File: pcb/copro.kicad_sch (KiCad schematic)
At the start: 6 parts, among them U10 74HC245, U2 ATmega1284-P, U6 74HC245, U7 74HC04, U8 74HC02, U9 74HC245

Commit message: WIP schematic
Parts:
- renumbered U8 to U37, U2 to U38, U10 to U39, U9 to U40, U6 to U41, U7 to U9
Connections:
- net VCC renamed +5V

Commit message: WIP PCB
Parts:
- renumbered U37 to U?, U41 to U?, U38 to U?, U39 to U?, U40 to U?, U9 to U?

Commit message: wip schematic
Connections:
- net +5V: now also U?.1 (A->B), U?.1 (A->B)
- net GND: no longer U?.1 (A->B), U?.1 (A->B)
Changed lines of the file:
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@@
-	(wire
-		(pts
-			(xy 107.95 93.98) (xy 107.95 97.79)
-		)
-		(stroke
-			(width 0)
-			(type default)
-		)
-	)
 	(wire
 		(pts
@@
 		(pts
 			(xy 50.8 154.94) (xy 53.34 154.94)
-		)
-		(stroke
-			(width 0)
-			(type default)
-		)
-	)
-	(wire
-		(pts
-			(xy 69.85 58.42) (xy 69.85 54.61)
 		)
 		(stroke
@@
 	)
 	(symbol
-		(lib_id "power:GND")
-		(at 107.95 97.79 0)
-		(unit 1)
-		(exclude_from_sim no)
-		(in_bom yes)
-		(on_board yes)
-		(dnp no)
-		(property "Reference" "#PWR?"
-			(at 107.95 104.14 0)
-			(effects
-				(font
-					(size 1.27 1.27)
-				)
-				(hide yes)
-			)
-		)
-		(property "Value" "GND"
-			(at 107.95 101.6 0)
-			(effects
-				(font
-					(size 1.27 1.27)
-				)
-			)
-		)
-		(property "Footprint" ""
-			(at 107.95 97.79 0)
-			(effects
-				(font
-					(size 1.27 1.27)
-				)
-				(hide yes)
-			)
-		)
-		(property "Datasheet" ""
-			(at 107.95 97.79 0)
-			(effects
-				(font
-					(size 1.27 1.27)
-				)
-				(hide yes)
-			)
-		)
-		(property "Description" "Power symbol creates a global label with name \"GND\" , ground"
-			(at 107.95 97.79 0)
-			(effects
-				(font
-					(size 1.27 1.27)
-				)
-				(hide yes)
-			)
-		)
-		(pin "1"
-		)
-		(instances
-			(project "fnx51"
-				(path "/e63e39d7-6ac0-4ffd-8aa3-1841a4541b55/90e1f016-3c60-4383-aa8d-def9977ac47b/81e744bc-21ac-4a4e-ae92-db4ae42ab216"
-					(reference "#PWR?")
-					(unit 1)
-				)
-			)
-		)
-	)
-	(symbol
 		(lib_id "MCU_Microchip_ATmega:ATmega1284-P")
 		(at 50.8 207.01 0)
@@
 	)
 	(symbol
-		(lib_id "power:GND")
-		(at 69.85 58.42 0)
+		(lib_id "power:+5V")
+		(at 107.95 93.98 0)
 		(unit 1)
 		(exclude_from_sim no)
@@
 		(on_board yes)
 		(dnp no)
-		(property "Reference" "#PWR?"
-			(at 69.85 64.77 0)
-			(effects
-				(font
-					(size 1.27 1.27)
-				)
-				(hide yes)
-			)
-		)
-		(property "Value" "GND"
-			(at 69.85 62.23 0)
+		(property "Reference" "#PWR04"
+			(at 107.95 97.79 0)
+			(effects
+				(font
+					(size 1.27 1.27)
+				)
+				(hide yes)
+			)
+		)
+		(property "Value" "+5V"
+			(at 104.14 92.71 0)
 			(effects
 				(font
@@
 		)
 		(property "Footprint" ""
-			(at 69.85 58.42 0)
+			(at 107.95 93.98 0)
 			(effects
 				(font
@@
 		)
 		(property "Datasheet" ""
-			(at 69.85 58.42 0)
-			(effects
-				(font
-					(size 1.27 1.27)
-				)
-				(hide yes)
-			)
-		)
-		(property "Description" "Power symbol creates a global label with name \"GND\" , ground"
-			(at 69.85 58.42 0)
+			(at 107.95 93.98 0)
+			(effects
+				(font
+					(size 1.27 1.27)
+				)
+				(hide yes)
+			)
+		)
+		(property "Description" "Power symbol creates a global label with name \"+5V\""
+			(at 107.95 93.98 0)
 			(effects
 				(font
@@
 			(project "fnx51"
 				(path "/e63e39d7-6ac0-4ffd-8aa3-1841a4541b55/90e1f016-3c60-4383-aa8d-def9977ac47b/81e744bc-21ac-4a4e-ae92-db4ae42ab216"
-					(reference "#PWR?")
+					(reference "#PWR04")
 					(unit 1)
 				)
@@
 				)
 			)
+		)
+	)
+	(symbol
+		(lib_id "power:+5V")
+		(at 69.85 54.61 0)
+		(unit 1)
+		(exclude_from_sim no)
+		(in_bom yes)
+		(on_board yes)
+		(dnp no)
+		(property "Reference" "#PWR03"
+			(at 69.85 58.42 0)
+			(effects
+				(font
+					(size 1.27 1.27)
+				)
+				(hide yes)
+			)
+		)
+		(property "Value" "+5V"
+			(at 66.04 53.34 0)
+			(effects
+				(font
+					(size 1.27 1.27)
+				)
+			)
+		)
+		(property "Footprint" ""
+			(at 69.85 54.61 0)
+			(effects
+				(font
+					(size 1.27 1.27)
+				)
+				(hide yes)
+			)
+		)
+		(property "Datasheet" ""
+			(at 69.85 54.61 0)
+			(effects
+				(font
+					(size 1.27 1.27)
+				)
+				(hide yes)
+			)
+		)
+		(property "Description" "Power symbol creates a global label with name \"+5V\""
+			(at 69.85 54.61 0)
+			(effects
+				(font
+					(size 1.27 1.27)
+				)
+				(hide yes)
+			)
+		)
+		(pin "1"
+		)
+		(instances
+			(project "fnx51"
+				(path "/e63e39d7-6ac0-4ffd-8aa3-1841a4541b55/90e1f016-3c60-4383-aa8d-def9977ac47b/81e744bc-21ac-4a4e-ae92-db4ae42ab216"
+					(reference "#PWR03")
+					(unit 1)
+				)
+			)

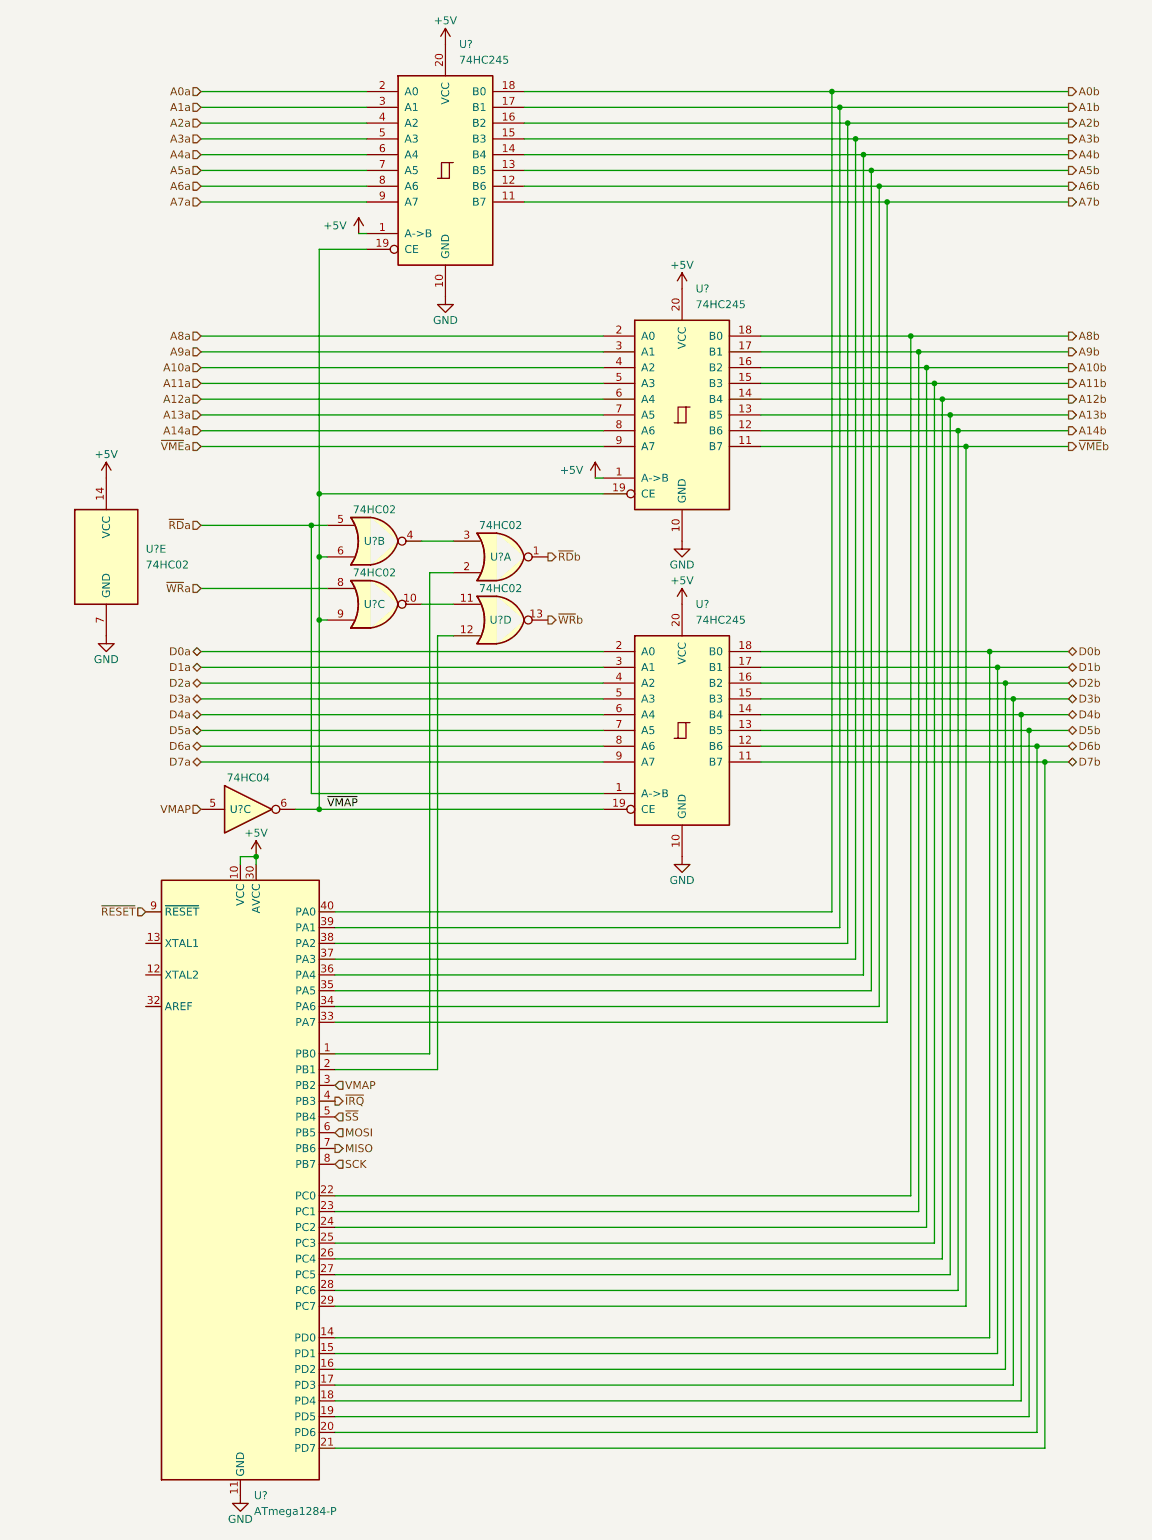
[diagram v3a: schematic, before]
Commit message: PCB: add reset circuit, xtal
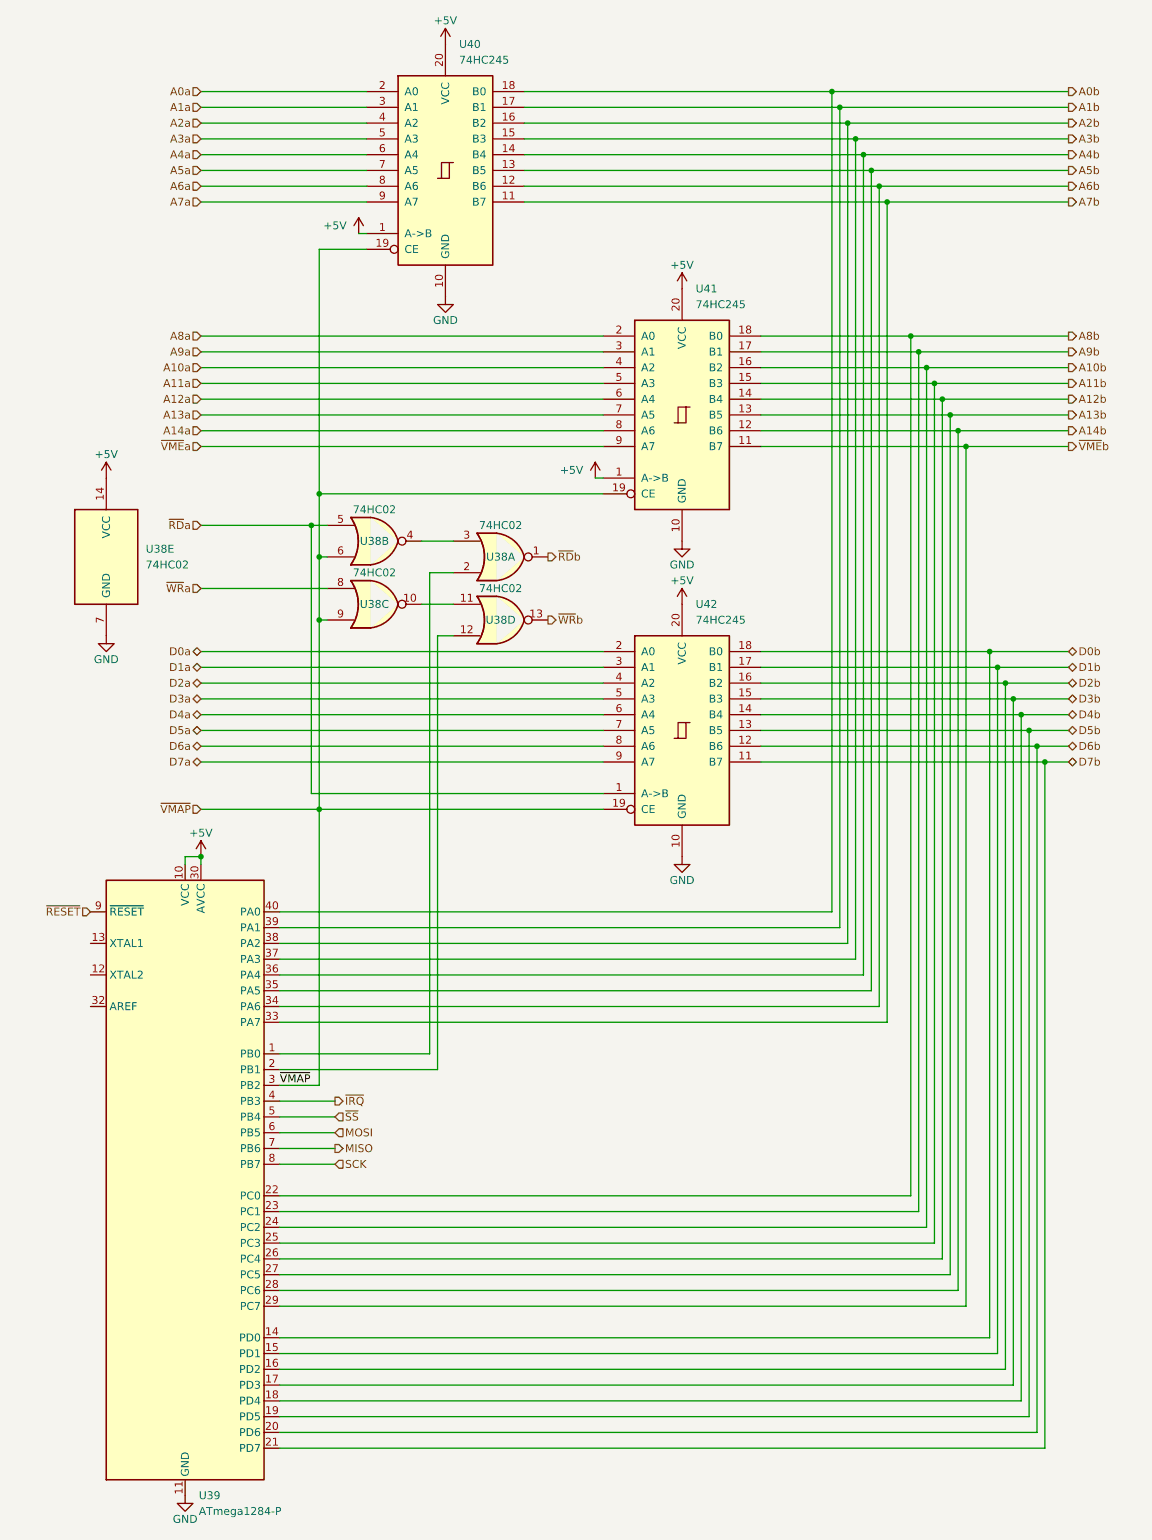
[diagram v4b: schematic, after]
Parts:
- removed U?: 74HC04, symbol 74xx:74HC04
- gave numbers to parts that had none: 5
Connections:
- net VMAP is gone; now on net ~{VMAP}: U39.3 (PB2)
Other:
- moved on the sheet: U39

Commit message: WIP schematic
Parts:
- renumbered U38 to U39, U39 to U40, U40 to U41, U41 to U42, U42 to U43
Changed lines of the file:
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@@
 		(on_board yes)
 		(dnp no)
-		(property "Reference" "U38"
+		(property "Reference" "U39"
 			(at 72.39 104.14 0)
 			(effects
@@
 			(project ""
 				(path "/e63e39d7-6ac0-4ffd-8aa3-1841a4541b55/90e1f016-3c60-4383-aa8d-def9977ac47b/81e744bc-21ac-4a4e-ae92-db4ae42ab216"
-					(reference "U38")
+					(reference "U39")
 					(unit 2)
 				)
@@
 		(on_board yes)
 		(dnp no)
-		(property "Reference" "U38"
+		(property "Reference" "U39"
 			(at 92.71 116.84 0)
 			(effects
@@
 			(project ""
 				(path "/e63e39d7-6ac0-4ffd-8aa3-1841a4541b55/90e1f016-3c60-4383-aa8d-def9977ac47b/81e744bc-21ac-4a4e-ae92-db4ae42ab216"
-					(reference "U38")
+					(reference "U39")
 					(unit 4)
 				)
@@
 		(on_board yes)
 		(dnp no)
-		(property "Reference" "#PWR0132"
+		(property "Reference" "#PWR0147"
 			(at 121.92 161.29 0)
 			(effects
@@
 			(project ""
 				(path "/e63e39d7-6ac0-4ffd-8aa3-1841a4541b55/90e1f016-3c60-4383-aa8d-def9977ac47b/81e744bc-21ac-4a4e-ae92-db4ae42ab216"
-					(reference "#PWR0132")
+					(reference "#PWR0147")
 					(unit 1)
 				)
@@
 		(on_board yes)
 		(dnp no)
-		(property "Reference" "#PWR0127"
+		(property "Reference" "#PWR0142"
 			(at 83.82 71.12 0)
 			(effects
@@
 			(project "fnx51"
 				(path "/e63e39d7-6ac0-4ffd-8aa3-1841a4541b55/90e1f016-3c60-4383-aa8d-def9977ac47b/81e744bc-21ac-4a4e-ae92-db4ae42ab216"
-					(reference "#PWR0127")
+					(reference "#PWR0142")
 					(unit 1)
 				)
@@
 		(on_board yes)
 		(dnp no)
-		(property "Reference" "U38"
+		(property "Reference" "U39"
 			(at 72.39 114.3 0)
 			(effects
@@
 			(project ""
 				(path "/e63e39d7-6ac0-4ffd-8aa3-1841a4541b55/90e1f016-3c60-4383-aa8d-def9977ac47b/81e744bc-21ac-4a4e-ae92-db4ae42ab216"
-					(reference "U38")
+					(reference "U39")
 					(unit 3)
 				)
@@
 		(on_board yes)
 		(dnp no)
-		(property "Reference" "#PWR0130"
+		(property "Reference" "#PWR0145"
 			(at 121.92 110.49 0)
 			(effects
@@
 			(project "fnx51"
 				(path "/e63e39d7-6ac0-4ffd-8aa3-1841a4541b55/90e1f016-3c60-4383-aa8d-def9977ac47b/81e744bc-21ac-4a4e-ae92-db4ae42ab216"
-					(reference "#PWR0130")
+					(reference "#PWR0145")
 					(unit 1)
 				)
@@
 		(dnp no)
 		(fields_autoplaced yes)
-		(property "Reference" "U42"
+		(property "Reference" "U43"
 			(at 124.1141 114.3 0)
 			(effects
@@
 			(project ""
 				(path "/e63e39d7-6ac0-4ffd-8aa3-1841a4541b55/90e1f016-3c60-4383-aa8d-def9977ac47b/81e744bc-21ac-4a4e-ae92-db4ae42ab216"
-					(reference "U42")
+					(reference "U43")
 					(unit 1)
 				)
@@
 		(dnp no)
 		(fields_autoplaced yes)
-		(property "Reference" "U39"
+		(property "Reference" "U40"
 			(at 44.1041 257.81 0)
 			(effects
@@
 			(project ""
 				(path "/e63e39d7-6ac0-4ffd-8aa3-1841a4541b55/90e1f016-3c60-4383-aa8d-def9977ac47b/81e744bc-21ac-4a4e-ae92-db4ae42ab216"
-					(reference "U39")
+					(reference "U40")
 					(unit 1)
 				)
@@
 		(on_board yes)
 		(dnp no)
-		(property "Reference" "#PWR0128"
+		(property "Reference" "#PWR0143"
 			(at 107.95 97.79 0)
 			(effects
@@
 			(project "fnx51"
 				(path "/e63e39d7-6ac0-4ffd-8aa3-1841a4541b55/90e1f016-3c60-4383-aa8d-def9977ac47b/81e744bc-21ac-4a4e-ae92-db4ae42ab216"
-					(reference "#PWR0128")
+					(reference "#PWR0143")
 					(unit 1)
 				)
@@
 		(on_board yes)
 		(dnp no)
-		(property "Reference" "#PWR0126"
+		(property "Reference" "#PWR0141"
 			(at 83.82 27.94 0)
 			(effects
@@
 			(project "fnx51"
 				(path "/e63e39d7-6ac0-4ffd-8aa3-1841a4541b55/90e1f016-3c60-4383-aa8d-def9977ac47b/81e744bc-21ac-4a4e-ae92-db4ae42ab216"
-					(reference "#PWR0126")
+					(reference "#PWR0141")
 					(unit 1)
 				)
@@
 		(on_board yes)
 		(dnp no)
-		(property "Reference" "U38"
+		(property "Reference" "U39"
 			(at 92.71 106.68 0)
 			(effects
@@
 			(project ""
 				(path "/e63e39d7-6ac0-4ffd-8aa3-1841a4541b55/90e1f016-3c60-4383-aa8d-def9977ac47b/81e744bc-21ac-4a4e-ae92-db4ae42ab216"
-					(reference "U38")
+					(reference "U39")
 					(unit 1)
 				)
@@
 		(on_board yes)
 		(dnp no)
-		(property "Reference" "#PWR0131"
+		(property "Reference" "#PWR0146"
 			(at 121.92 118.11 0)
 			(effects
@@
 			(project ""
 				(path "/e63e39d7-6ac0-4ffd-8aa3-1841a4541b55/90e1f016-3c60-4383-aa8d-def9977ac47b/81e744bc-21ac-4a4e-ae92-db4ae42ab216"
-					(reference "#PWR0131")
+					(reference "#PWR0146")
 					(unit 1)
 				)
@@
 		(dnp no)
 		(fields_autoplaced yes)
-		(property "Reference" "U40"
+		(property "Reference" "U41"
 			(at 86.0141 24.13 0)
 			(effects
@@
 			(project "fnx51"
 				(path "/e63e39d7-6ac0-4ffd-8aa3-1841a4541b55/90e1f016-3c60-4383-aa8d-def9977ac47b/81e744bc-21ac-4a4e-ae92-db4ae42ab216"
-					(reference "U40")
+					(reference "U41")
 					(unit 1)
 				)
@@
 		(dnp no)
 		(fields_autoplaced yes)
-		(property "Reference" "U38"
+		(property "Reference" "U39"
 			(at 35.56 105.4099 0)
 			(effects
@@
 			(project ""
 				(path "/e63e39d7-6ac0-4ffd-8aa3-1841a4541b55/90e1f016-3c60-4383-aa8d-def9977ac47b/81e744bc-21ac-4a4e-ae92-db4ae42ab216"
-					(reference "U38")
+					(reference "U39")
 					(unit 5)
 				)
@@
 		(on_board yes)
 		(dnp no)
-		(property "Reference" "#PWR0125"
+		(property "Reference" "#PWR0140"
 			(at 69.85 58.42 0)
 			(effects
@@
 			(project "fnx51"
 				(path "/e63e39d7-6ac0-4ffd-8aa3-1841a4541b55/90e1f016-3c60-4383-aa8d-def9977ac47b/81e744bc-21ac-4a4e-ae92-db4ae42ab216"
-					(reference "#PWR0125")
+					(reference "#PWR0140")
 					(unit 1)
 				)
@@
 		(on_board yes)
 		(dnp no)
-		(property "Reference" "#PWR0121"
+		(property "Reference" "#PWR0136"
 			(at 29.21 97.79 0)
 			(effects
@@
 			(project "fnx51"
 				(path "/e63e39d7-6ac0-4ffd-8aa3-1841a4541b55/90e1f016-3c60-4383-aa8d-def9977ac47b/81e744bc-21ac-4a4e-ae92-db4ae42ab216"
-					(reference "#PWR0121")
+					(reference "#PWR0136")
 					(unit 1)
 				)
@@
 		(dnp no)
 		(fields_autoplaced yes)
-		(property "Reference" "U41"
+		(property "Reference" "U42"
 			(at 124.1141 63.5 0)
 			(effects
@@
 			(project "fnx51"
 				(path "/e63e39d7-6ac0-4ffd-8aa3-1841a4541b55/90e1f016-3c60-4383-aa8d-def9977ac47b/81e744bc-21ac-4a4e-ae92-db4ae42ab216"
-					(reference "U41")
+					(reference "U42")
 					(unit 1)
 				)
@@
 		(on_board yes)
 		(dnp no)
-		(property "Reference" "#PWR0123"
+		(property "Reference" "#PWR0138"
 			(at 41.91 264.16 0)
 			(effects
@@
 			(project "fnx51"
 				(path "/e63e39d7-6ac0-4ffd-8aa3-1841a4541b55/90e1f016-3c60-4383-aa8d-def9977ac47b/81e744bc-21ac-4a4e-ae92-db4ae42ab216"
-					(reference "#PWR0123")
+					(reference "#PWR0138")
 					(unit 1)
 				)
@@
 		(on_board yes)
 		(dnp no)
-		(property "Reference" "#PWR0124"
+		(property "Reference" "#PWR0139"
 			(at 44.45 158.75 0)
 			(effects
@@
 			(project "fnx51"
 				(path "/e63e39d7-6ac0-4ffd-8aa3-1841a4541b55/90e1f016-3c60-4383-aa8d-def9977ac47b/81e744bc-21ac-4a4e-ae92-db4ae42ab216"
-					(reference "#PWR0124")
+					(reference "#PWR0139")
 					(unit 1)
 				)
@@
 		(on_board yes)
 		(dnp no)
-		(property "Reference" "#PWR0122"
+		(property "Reference" "#PWR0137"
 			(at 29.21 125.73 0)
 			(effects
@@
 			(project "fnx51"
 				(path "/e63e39d7-6ac0-4ffd-8aa3-1841a4541b55/90e1f016-3c60-4383-aa8d-def9977ac47b/81e744bc-21ac-4a4e-ae92-db4ae42ab216"
-					(reference "#PWR0122")
+					(reference "#PWR0137")
 					(unit 1)
 				)
@@
 		(on_board yes)
 		(dnp no)
-		(property "Reference" "#PWR0129"
+		(property "Reference" "#PWR0144"
 			(at 121.92 67.31 0)
 			(effects
@@
 			(project "fnx51"
 				(path "/e63e39d7-6ac0-4ffd-8aa3-1841a4541b55/90e1f016-3c60-4383-aa8d-def9977ac47b/81e744bc-21ac-4a4e-ae92-db4ae42ab216"
-					(reference "#PWR0129")
+					(reference "#PWR0144")
 					(unit 1)
 				)
